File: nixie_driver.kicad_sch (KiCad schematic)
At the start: 52 parts, among them Q1 MPSA92, Q10 MPSA92, Q11 MPSA92, Q12 MPSA92, Q2 MPSA92, Q3 MPSA92, Q4 MPSA92, Q5 MPSA92, Q6 MPSA92, Q7 MPSA92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

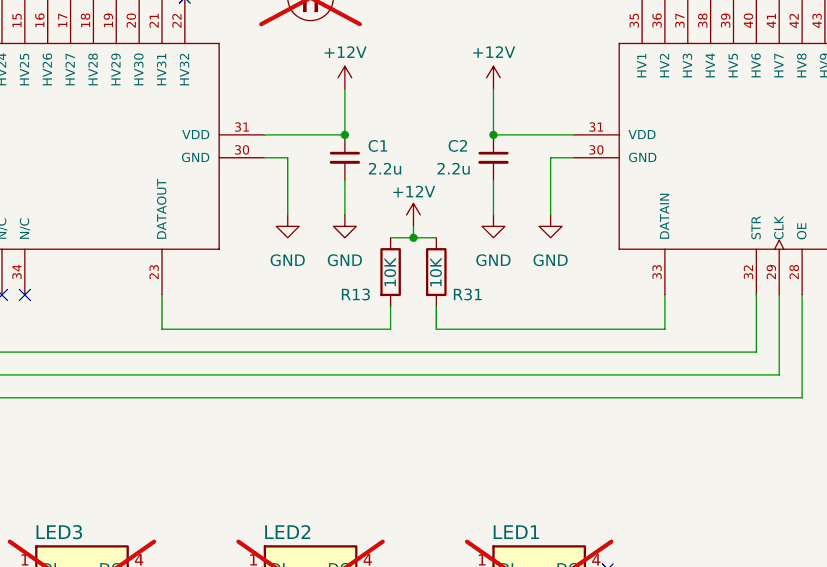
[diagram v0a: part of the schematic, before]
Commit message: fixed pull-ups
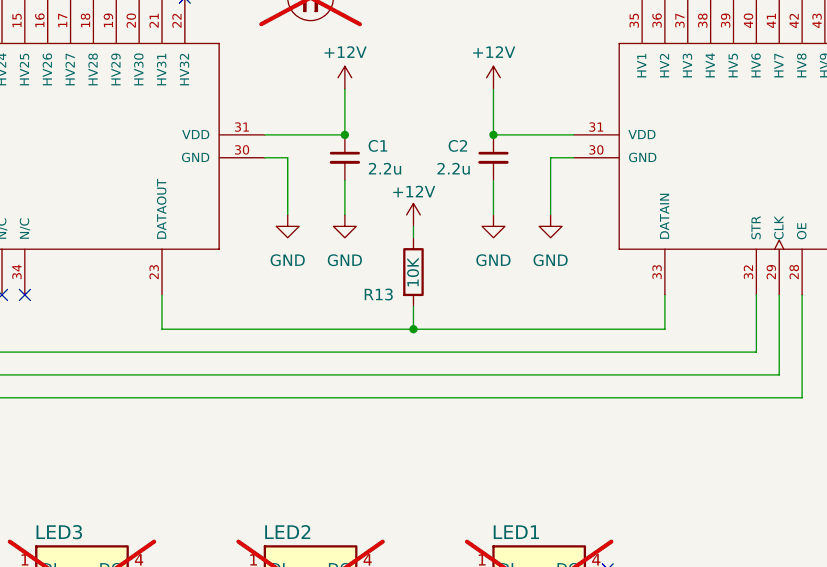
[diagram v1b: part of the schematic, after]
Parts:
- removed R31: 10K, Resistor_SMD:R_1206_3216Metric, symbol Device:R
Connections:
- net at U2.33 (DATAIN): now also R13.2, U1.23 (DATAOUT)
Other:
- moved on the sheet: R13
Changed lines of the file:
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@@
 	)
 	(junction
-		(at 147.32 133.35)
-		(diameter 0)
-		(color 0 0 0 0)
-	)
-	(junction
 		(at 39.37 38.1)
 		(diameter 0)
@@
 	)
 	(junction
+		(at 147.32 143.51)
+		(diameter 0)
+		(color 0 0 0 0)
+	)
+	(junction
 		(at 214.63 38.1)
 		(diameter 0)
@@
 	(wire
 		(pts
-			(xy 149.86 140.97) (xy 149.86 143.51)
-		)
-		(stroke
-			(width 0)
-			(type default)
-		)
-	)
-	(wire
-		(pts
 			(xy 41.91 181.61) (xy 24.13 181.61)
 		)
@@
 	(wire
 		(pts
-			(xy 149.86 143.51) (xy 175.26 143.51)
+			(xy 147.32 143.51) (xy 175.26 143.51)
 		)
 		(stroke
@@
 	(wire
 		(pts
-			(xy 147.32 133.35) (xy 149.86 133.35)
-		)
-		(stroke
-			(width 0)
-			(type default)
-		)
-	)
-	(wire
-		(pts
 			(xy 125.73 184.15) (xy 125.73 181.61)
 		)
@@
 	(wire
 		(pts
-			(xy 119.38 143.51) (xy 144.78 143.51)
+			(xy 119.38 143.51) (xy 147.32 143.51)
 		)
 		(stroke
@@
 	(wire
 		(pts
-			(xy 144.78 140.97) (xy 144.78 143.51)
+			(xy 147.32 140.97) (xy 147.32 143.51)
 		)
 		(stroke
@@
 	(wire
 		(pts
-			(xy 147.32 133.35) (xy 144.78 133.35)
-		)
-		(stroke
-			(width 0)
-			(type default)
-		)
-	)
-	(wire
-		(pts
 			(xy 74.93 184.15) (xy 74.93 181.61)
 		)
@@
 	(symbol
 		(lib_id "Device:R")
-		(at 144.78 137.16 0)
+		(at 147.32 137.16 0)
 		(unit 1)
 		(exclude_from_sim no)
@@
 		(dnp no)
 		(property "Reference" "R13"
-			(at 139.192 139.7 0)
+			(at 141.732 139.7 0)
 			(effects
 				(font
@@
 		)
 		(property "Value" "10K"
-			(at 144.78 138.938 90)
+			(at 147.32 138.938 90)
 			(effects
 				(font
@@
 		)
 		(property "Footprint" "Resistor_SMD:R_1206_3216Metric"
-			(at 143.002 137.16 90)
+			(at 145.542 137.16 90)
 			(effects
 				(font
@@
 		)
 		(property "Datasheet" "~"
-			(at 144.78 137.16 0)
+			(at 147.32 137.16 0)
 			(effects
 				(font
@@
 		)
 		(property "Description" ""
-			(at 144.78 137.16 0)
+			(at 147.32 137.16 0)
 			(effects
 				(font
@@
 		)
 		(property "MPN" "CRCW120610K0FKEA"
-			(at 144.78 137.16 0)
+			(at 147.32 137.16 0)
 			(effects
 				(font
@@
 		)
 		(property "Manufacturer_Part_Number" ""
-			(at 144.78 137.16 0)
+			(at 147.32 137.16 0)
 			(effects
 				(font
@@
 		)
 		(property "Reichelt" ""
-			(at 144.78 137.16 0)
+			(at 147.32 137.16 0)
 			(effects
 				(font
@@
 		)
 		(property "Sim.Device" ""
-			(at 144.78 137.16 0)
+			(at 147.32 137.16 0)
 			(effects
 				(font
@@
 		)
 		(property "Sim.Pins" ""
-			(at 144.78 137.16 0)
+			(at 147.32 137.16 0)
 			(effects
 				(font
@@
 		)
 		(property "manf#" ""
-			(at 144.78 137.16 0)
+			(at 147.32 137.16 0)
 			(effects
 				(font
@@
 					(unit 1)
 				)
-			)
-		)
-	)
-	(symbol
-		(lib_id "Device:R")
-		(at 149.86 137.16 0)
-		(unit 1)
-		(exclude_from_sim no)
-		(in_bom yes)
-		(on_board yes)
-		(dnp no)
-		(property "Reference" "R31"
-			(at 151.638 139.7 0)
-			(effects
-				(font
-					(size 1.27 1.27)
-				)
-				(justify left)
-			)
-		)
-		(property "Value" "10K"
-			(at 149.86 138.938 90)
-			(effects
-				(font
-					(size 1.27 1.27)
-				)
-				(justify left)
-			)
-		)
-		(property "Footprint" "Resistor_SMD:R_1206_3216Metric"
-			(at 148.082 137.16 90)
-			(effects
-				(font
-					(size 1.27 1.27)
-				)
-				(hide yes)
-			)
-		)
-		(property "Datasheet" "~"
-			(at 149.86 137.16 0)
-			(effects
-				(font
-					(size 1.27 1.27)
-				)
-				(hide yes)
-			)
-		)
-		(property "Description" ""
-			(at 149.86 137.16 0)
-			(effects
-				(font
-					(size 1.27 1.27)
-				)
-				(hide yes)
-			)
-		)
-		(property "MPN" "CRCW120610K0FKEA"
-			(at 149.86 137.16 0)
-			(effects
-				(font
-					(size 1.27 1.27)
-				)
-				(hide yes)
-			)
-		)
-		(property "Manufacturer_Part_Number" ""
-			(at 149.86 137.16 0)
-			(effects
-				(font
-					(size 1.27 1.27)
-				)
-				(hide yes)
-			)
-		)
-		(property "Reichelt" ""
-			(at 149.86 137.16 0)
-			(effects
-				(font
-					(size 1.27 1.27)
-				)
-				(hide yes)
-			)
-		)
-		(property "Sim.Device" ""
-			(at 149.86 137.16 0)
-			(effects
-				(font
-					(size 1.27 1.27)
-				)
-				(hide yes)
-			)
-		)
-		(property "Sim.Pins" ""
-			(at 149.86 137.16 0)
-			(effects
-				(font
-					(size 1.27 1.27)
-				)
-				(hide yes)
-			)
-		)
-		(property "manf#" ""
-			(at 149.86 137.16 0)
-			(effects
-				(font
-					(size 1.27 1.27)
-				)
-				(hide yes)
-			)
-		)
-		(pin "1"
-		)
-		(pin "2"
-		)
-		(instances
-			(project "nixie_clock_design"
-				(path "/a685e357-0c48-4039-9775-db3bc428cd49/06b98f29-c4b1-45e0-855d-428084a71670"
-					(reference "R31")
-					(unit 1)
-				)

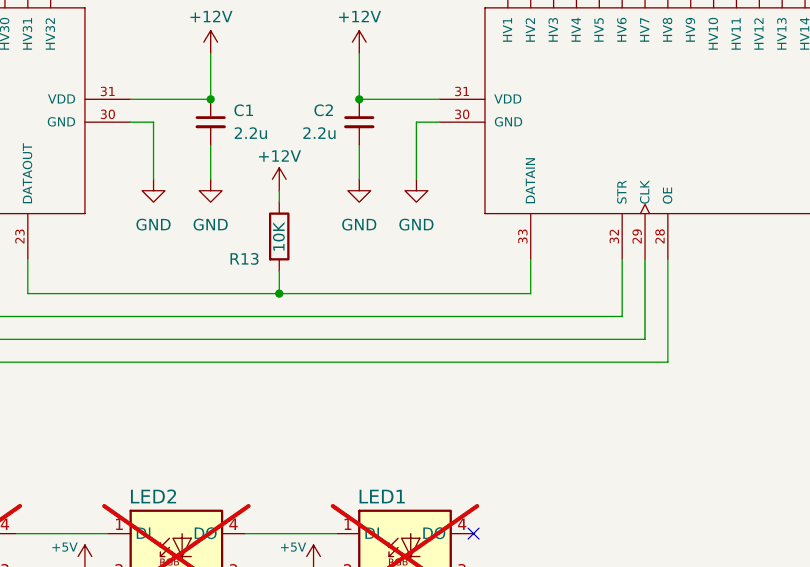
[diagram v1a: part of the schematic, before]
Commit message: added HV5122 data line shunt
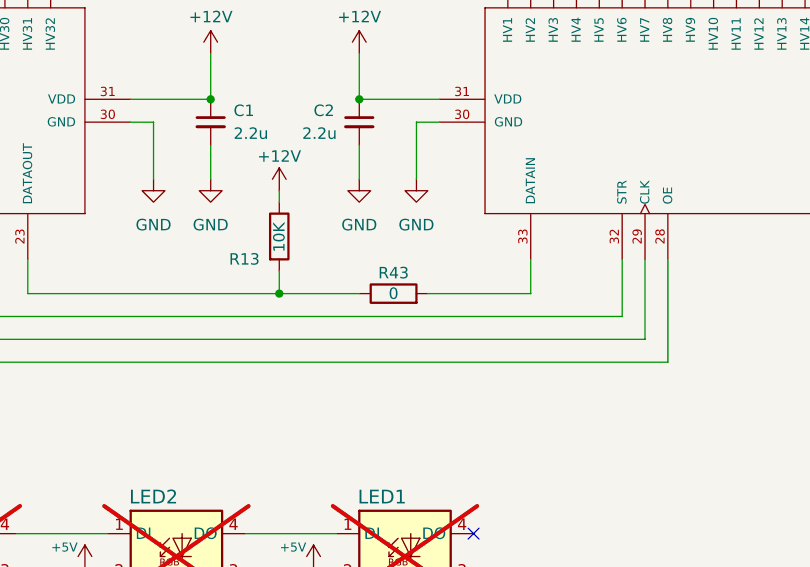
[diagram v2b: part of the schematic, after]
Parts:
- added R43: 0, Resistor_SMD:R_0603_1608Metric, symbol Device:R
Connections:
- net at R13.2, U1.23 (DATAOUT): now also R43.1; no longer U2.33 (DATAIN)
- new net: R43.2, U2.33 (DATAIN)
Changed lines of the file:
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@@
 	)
 	(junction
-		(at 171.45 38.1)
+		(at 147.32 143.51)
 		(diameter 0)
 		(color 0 0 0 0)
 	)
 	(junction
-		(at 125.73 24.13)
+		(at 171.45 38.1)
 		(diameter 0)
 		(color 0 0 0 0)
 	)
 	(junction
-		(at 151.13 181.61)
+		(at 125.73 24.13)
 		(diameter 0)
 		(color 0 0 0 0)
 	)
 	(junction
-		(at 147.32 143.51)
+		(at 151.13 181.61)
 		(diameter 0)
 		(color 0 0 0 0)
@@
 	(wire
 		(pts
-			(xy 147.32 143.51) (xy 175.26 143.51)
+			(xy 147.32 143.51) (xy 156.21 143.51)
 		)
 		(stroke
@@
 	(wire
 		(pts
+			(xy 163.83 143.51) (xy 175.26 143.51)
+		)
+		(stroke
+			(width 0)
+			(type default)
+		)
+	)
+	(wire
+		(pts
 			(xy 49.53 184.15) (xy 49.53 181.61)
 		)
@@
 	(wire
 		(pts
+			(xy 119.38 143.51) (xy 147.32 143.51)
+		)
+		(stroke
+			(width 0)
+			(type default)
+		)
+	)
+	(wire
+		(pts
 			(xy 120.65 86.36) (xy 120.65 93.98)
 		)
@@
 	(wire
 		(pts
-			(xy 119.38 143.51) (xy 147.32 143.51)
-		)
-		(stroke
-			(width 0)
-			(type default)
-		)
-	)
-	(wire
-		(pts
 			(xy 92.71 181.61) (xy 74.93 181.61)
 		)
@@
 					(unit 1)
 				)
+			)
+		)
+	)
+	(symbol
+		(lib_id "Device:R")
+		(at 160.02 143.51 90)
+		(unit 1)
+		(exclude_from_sim no)
+		(in_bom yes)
+		(on_board yes)
+		(dnp no)
+		(property "Reference" "R43"
+			(at 160.02 141.224 90)
+			(effects
+				(font
+					(size 1.27 1.27)
+				)
+			)
+		)
+		(property "Value" "0"
+			(at 160.02 143.51 90)
+			(effects
+				(font
+					(size 1.27 1.27)
+				)
+			)
+		)
+		(property "Footprint" "Resistor_SMD:R_0603_1608Metric"
+			(at 160.02 145.288 90)
+			(effects
+				(font
+					(size 1.27 1.27)
+				)
+				(hide yes)
+			)
+		)
+		(property "Datasheet" "~"
+			(at 160.02 143.51 0)
+			(effects
+				(font
+					(size 1.27 1.27)
+				)
+				(hide yes)
+			)
+		)
+		(property "Description" "Resistor"
+			(at 160.02 143.51 0)
+			(effects
+				(font
+					(size 1.27 1.27)
+				)
+				(hide yes)
+			)
+		)
+		(property "MPN" "MCT06030Z0000ZPW00"
+			(at 160.02 143.51 90)
+			(effects
+				(font
+					(size 1.27 1.27)
+				)
+				(hide yes)
+			)
+		)
+		(pin "1"
+		)
+		(pin "2"
+		)
+		(instances
+			(project "nixie_clock_design"
+				(path "/a685e357-0c48-4039-9775-db3bc428cd49/06b98f29-c4b1-45e0-855d-428084a71670"
+					(reference "R43")
+					(unit 1)
+				)

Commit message: updated lcsc parts
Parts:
- C1, C10, C11, C2, C26, C27, C7, C8: LCSC Part Number (none) -> C19110
- Q1, Q10, Q11, Q12, Q2, Q3, Q4, Q5, Q6, Q7, Q8, Q9: LCSC Part Number (none) -> C305412
- R1, R2, R3, R4, R5, R6: LCSC Part Number (none) -> C137312
- R10, R11, R12, R7, R8, R9: LCSC Part Number (none) -> C25374
- R13: LCSC Part Number (none) -> C17902
- R40, R41: LCSC Part Number (none) -> C22875
- R43: LCSC Part Number (none) -> C21189
- U1, U2: LCSC Part Number (none) -> C646051
